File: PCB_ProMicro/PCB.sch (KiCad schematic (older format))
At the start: 104 parts, among them J1 USB-C, J2 BATT, J3 USB, SW1 SW_Push, SW10 SW_Push, SW11 SW_Push, SW12 SW_Push, SW13 SW_Push, SW14 SW_Push, SW15 SW_Push, SW16 SW_Push, SW17 SW_Push, SW18 SW_Push, SW19 SW_Push, SW2 SW_Push, SW20 SW_Push, SW21 SW_Push, SW22 SW_Push, SW23 SW_Push, SW24 SW_Push, SW25 SW_Push, SW26 SW_Push, SW27 SW_Push, SW28 SW_Push, SW29 SW_Push, SW3 SW_Push, SW30 SW_Push, SW31 SW_Push, SW32 SW_Push, SW33 SW_Push, SW34 SW_Push, SW35 SW_Push, SW36 SW_Push, SW37 SW_Push, SW38 SW_Push, SW39 SW_Push, SW4 SW_Push, SW40 SW_Push, SW41 SW_Push, SW42 SW_Push, SW43 SW_Push, SW44 SW_Push, SW45 SW_Push, SW46 SW_Push, SW47 SW_Push, SW48 SW_Push, SW49 SW_Push, SW5 SW_Push, SW6 SW_Push, SW7 SW_Push, SW8 SW_Push, SW9 SW_Push, U1 ProMicro

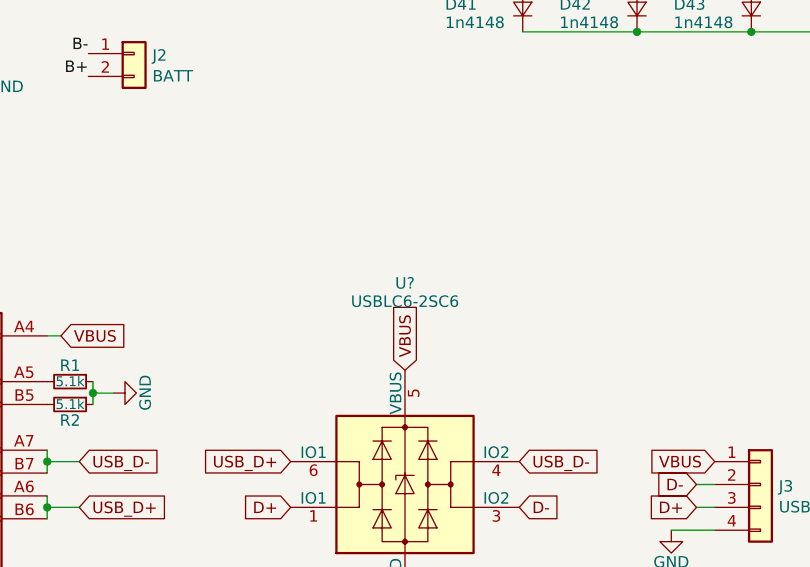
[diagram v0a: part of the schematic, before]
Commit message: Assign PCB footprint to schematic symbols
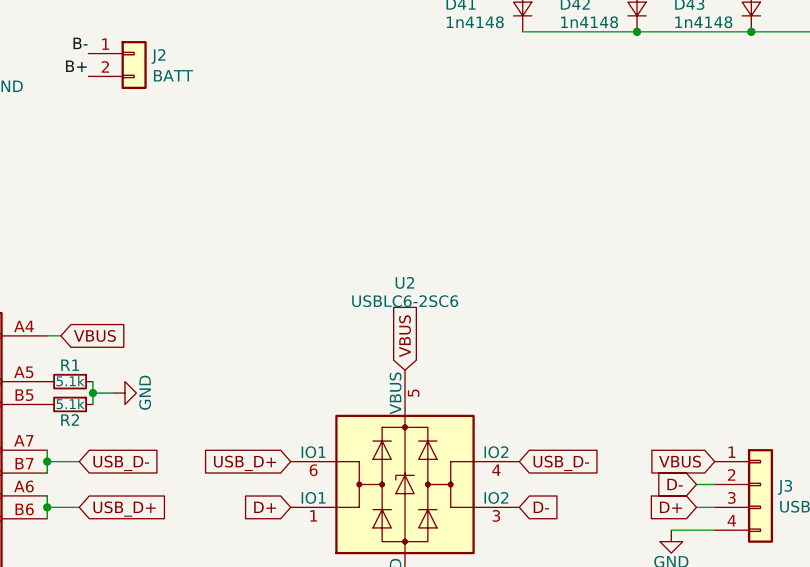
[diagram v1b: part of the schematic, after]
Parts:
- J1: footprint (none) -> Type-C:HRO-TYPE-C-31-M-12-HandSoldering
- J2: footprint (none) -> Infinity:BattPin_2mm
- J3: footprint (none) -> Infinity:USB-C-Pin-2mm
- R1, R2: footprint (none) -> Resistor_SMD:R_0603_1608Metric
- SW41, SW42, SW43, SW46, SW47, SW48: footprint Infinity:SW_MxHotswap_1.75u -> Infinity:SW_MxHotswap_1.5u
- SW44: footprint Infinity:SW_MxHotswap_1.75u -> Infinity:SW_MxHotswap_2.25u
- SW45: footprint Infinity:SW_MxHotswap_1.75u -> Infinity:SW_MxHotswap_2.75u
- U1: footprint (none) -> Infinity:ProMicro_26pin
- gave numbers to parts that had none: 1
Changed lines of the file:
@@
 F 0 "SW41" H 4100 2873 50  0000 C CNN
 F 1 "SW_Push" H 4100 2874 50  0001 C CNN
-F 2 "Infinity:SW_MxHotswap_1.75u" H 4100 2880 50  0001 C CNN
+F 2 "Infinity:SW_MxHotswap_1.5u" H 4100 2880 50  0001 C CNN
 F 3 "~" H 4100 2880 50  0001 C CNN
 	1    4100 2680
@@
 F 0 "SW42" H 4600 2873 50  0000 C CNN
 F 1 "SW_Push" H 4600 2874 50  0001 C CNN
-F 2 "Infinity:SW_MxHotswap_1.75u" H 4600 2880 50  0001 C CNN
+F 2 "Infinity:SW_MxHotswap_1.5u" H 4600 2880 50  0001 C CNN
 F 3 "~" H 4600 2880 50  0001 C CNN
 	1    4600 2680
@@
 F 0 "SW43" H 5100 2873 50  0000 C CNN
 F 1 "SW_Push" H 5100 2874 50  0001 C CNN
-F 2 "Infinity:SW_MxHotswap_1.75u" H 5100 2880 50  0001 C CNN
+F 2 "Infinity:SW_MxHotswap_1.5u" H 5100 2880 50  0001 C CNN
 F 3 "~" H 5100 2880 50  0001 C CNN
 	1    5100 2680
@@
 F 0 "SW44" H 6100 2873 50  0000 C CNN
 F 1 "SW_Push" H 6100 2874 50  0001 C CNN
-F 2 "Infinity:SW_MxHotswap_1.75u" H 6100 2880 50  0001 C CNN
+F 2 "Infinity:SW_MxHotswap_2.25u" H 6100 2880 50  0001 C CNN
 F 3 "~" H 6100 2880 50  0001 C CNN
 	1    6100 2680
@@
 F 0 "SW45" H 7600 2873 50  0000 C CNN
 F 1 "SW_Push" H 7600 2874 50  0001 C CNN
-F 2 "Infinity:SW_MxHotswap_1.75u" H 7600 2880 50  0001 C CNN
+F 2 "Infinity:SW_MxHotswap_2.75u" H 7600 2880 50  0001 C CNN
 F 3 "~" H 7600 2880 50  0001 C CNN
 	1    7600 2680
@@
 F 0 "SW46" H 8600 2873 50  0000 C CNN
 F 1 "SW_Push" H 8600 2874 50  0001 C CNN
-F 2 "Infinity:SW_MxHotswap_1.75u" H 8600 2880 50  0001 C CNN
+F 2 "Infinity:SW_MxHotswap_1.5u" H 8600 2880 50  0001 C CNN
 F 3 "~" H 8600 2880 50  0001 C CNN
 	1    8600 2680
@@
 F 0 "SW47" H 9100 2873 50  0000 C CNN
 F 1 "SW_Push" H 9100 2874 50  0001 C CNN
-F 2 "Infinity:SW_MxHotswap_1.75u" H 9100 2880 50  0001 C CNN
+F 2 "Infinity:SW_MxHotswap_1.5u" H 9100 2880 50  0001 C CNN
 F 3 "~" H 9100 2880 50  0001 C CNN
 	1    9100 2680
@@
 F 0 "SW48" H 10100 2873 50  0000 C CNN
 F 1 "SW_Push" H 10100 2874 50  0001 C CNN
-F 2 "Infinity:SW_MxHotswap_1.75u" H 10100 2880 50  0001 C CNN
+F 2 "Infinity:SW_MxHotswap_1.5u" H 10100 2880 50  0001 C CNN
 F 3 "~" H 10100 2880 50  0001 C CNN
 	1    10100 2680
@@
 F 0 "U1" H 2130 3157 60  0000 C CNN
 F 1 "ProMicro" H 2130 3070 60  0000 C CNN
-F 2 "" H 2230 1070 60  0000 C CNN
+F 2 "Infinity:ProMicro_26pin" H 2230 1070 60  0001 C CNN
 F 3 "" H 2230 1070 60  0000 C CNN
 	1    2130 2120
@@
 F 0 "J2" H 2680 2967 50  0000 L CNN
 F 1 "BATT" H 2680 2876 50  0000 L CNN
-F 2 "" H 2600 2975 50  0001 C CNN
+F 2 "Infinity:BattPin_2mm" H 2600 2975 50  0001 C CNN
 F 3 "~" H 2600 2975 50  0001 C CNN
 	1    2600 2975
@@
 F 0 "J1" H 1727 5677 50  0000 C CNN
 F 1 "USB-C" H 1727 5586 50  0000 C CNN
-F 2 "" H 1770 4810 50  0001 C CNN
+F 2 "Type-C:HRO-TYPE-C-31-M-12-HandSoldering" H 1770 4810 50  0001 C CNN
 F 3 "https://www.usb.org/sites/default/files/documents/usb_type-c.zip" H 1770 4810 50  0001 C CNN
 	1    1620 4810
@@
 	2220 4960 2220 5010
 $Comp
-L power:GND #PWR?
+L power:GND #PWR0104
 U 1 1 5EDC59F6
 P 1620 5710
-F 0 "#PWR?" H 1620 5460 50  0001 C CNN
+F 0 "#PWR0104" H 1620 5460 50  0001 C CNN
 F 1 "GND" H 1620 5565 50  0000 C CNN
 F 2 "" H 1620 5710 50  0001 C CNN
@@
 F 0 "R1" V 2250 4410 50  0000 C CNN
 F 1 "5.1k" V 2320 4410 43  0000 C CNN
-F 2 "" H 2320 4410 50  0001 C CNN
+F 2 "Resistor_SMD:R_0603_1608Metric" H 2320 4410 50  0001 C CNN
 F 3 "~" H 2320 4410 50  0001 C CNN
 	1    2320 4410
@@
 F 0 "R2" V 2390 4510 50  0000 C CNN
 F 1 "5.1k" V 2320 4510 43  0000 C CNN
-F 2 "" H 2320 4510 50  0001 C CNN
+F 2 "Resistor_SMD:R_0603_1608Metric" H 2320 4510 50  0001 C CNN
 F 3 "~" H 2320 4510 50  0001 C CNN
 	1    2320 4510
@@
 $EndComp
 $Comp
-L power:GND #PWR?
+L power:GND #PWR0105
 U 1 1 5EDCBE4E
 P 2510 4460
-F 0 "#PWR?" H 2510 4210 50  0001 C CNN
+F 0 "#PWR0105" H 2510 4210 50  0001 C CNN
 F 1 "GND" H 2590 4320 50  0000 R CNN
 F 2 "" H 2510 4460 50  0001 C CNN
@@
 NoConn ~ 2220 5410
 $Comp
-L Power_Protection:USBLC6-2SC6 U?
+L Power_Protection:USBLC6-2SC6 U2
 U 1 1 5EDE97BF
 P 3785 4860
-F 0 "U?" H 3785 5740 50  0000 C CNN
+F 0 "U2" H 3785 5740 50  0000 C CNN
 F 1 "USBLC6-2SC6" H 3785 5660 50  0000 C CNN
 F 2 "Package_TO_SOT_SMD:SOT-23-6" H 3035 5260 50  0001 C CNN
@@
 D-
 $Comp
-L power:GND #PWR?
+L power:GND #PWR0106
 U 1 1 5EDF1287
 P 3785 5360
-F 0 "#PWR?" H 3785 5110 50  0001 C CNN
+F 0 "#PWR0106" H 3785 5110 50  0001 C CNN
 F 1 "GND" H 3785 5220 50  0000 C CNN
 F 2 "" H 3785 5360 50  0001 C CNN
@@
 F 0 "J3" H 5420 4852 50  0000 L CNN
 F 1 "USB" H 5420 4761 50  0000 L CNN
-F 2 "" H 5340 4860 50  0001 C CNN
+F 2 "Infinity:USB-C-Pin-2mm" H 5340 4860 50  0001 C CNN
 F 3 "~" H 5340 4860 50  0001 C CNN
 	1    5340 4860
@@
 	5060 4860 5140 4860
 $Comp
-L power:GND #PWR?
+L power:GND #PWR0107
 U 1 1 5EE00720
 P 4950 5060
-F 0 "#PWR?" H 4950 4810 50  0001 C CNN
+F 0 "#PWR0107" H 4950 4810 50  0001 C CNN
 F 1 "GND" H 4950 4920 50  0000 C CNN
 F 2 "" H 4950 5060 50  0001 C CNN
